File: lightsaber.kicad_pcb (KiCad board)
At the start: 2 copper layers, 31.5 x 127.8 mm, 9 parts, among them SW1 Button, SW2 POWER, U1 C3 Pico

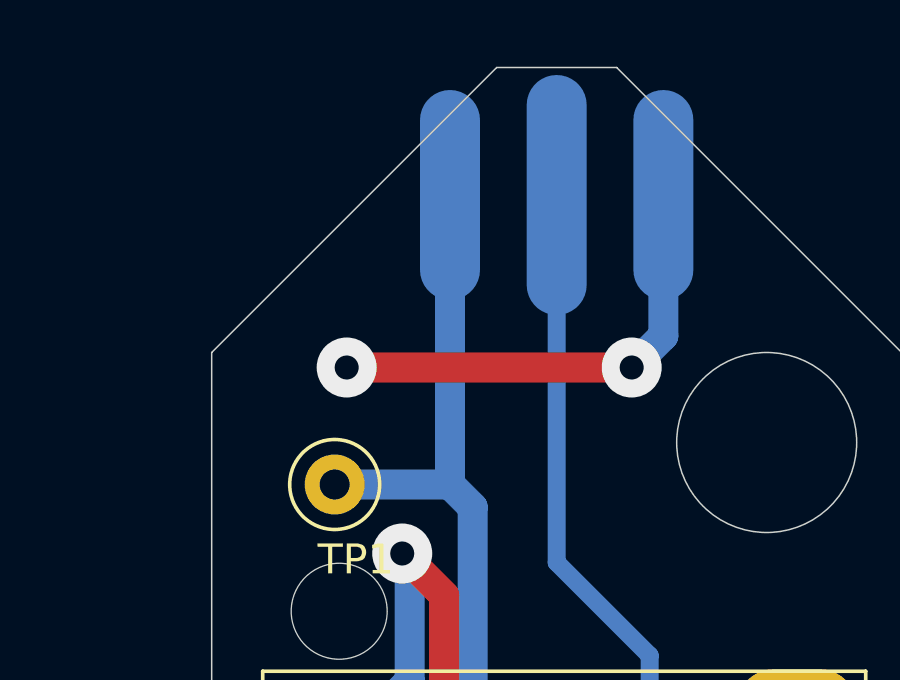
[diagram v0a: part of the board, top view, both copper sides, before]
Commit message: Make sure that the neopixel does not drain the battery so use 3V3 instead of VBAT
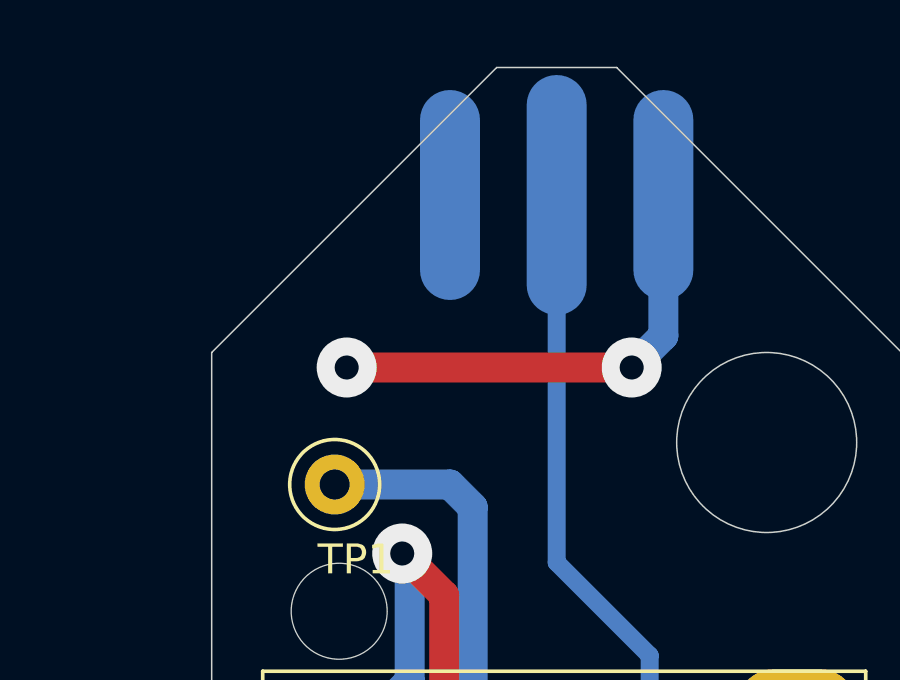
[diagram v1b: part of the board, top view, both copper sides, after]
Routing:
- net +4V: track 27.8 -> 18.1 mm
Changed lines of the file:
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@@
-	)
-	(segment
-		(start 116.944 48.65)
-		(end 116.944 39)
-		(width 1)
-		(layer "B.Cu")
-		(net 3)
 	)
 	(segment

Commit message: Specify light sensor and its resistor
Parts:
- R1: footprint OptoDevice:R_LDR_4.9x4.2mm_P2.54mm_Vertical -> OptoDevice:R_LDR_5.1x4.3mm_P3.4mm_Vertical
- R3: value 100k -> 47k
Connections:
- NP1 pad 1: +4V -> +3V3

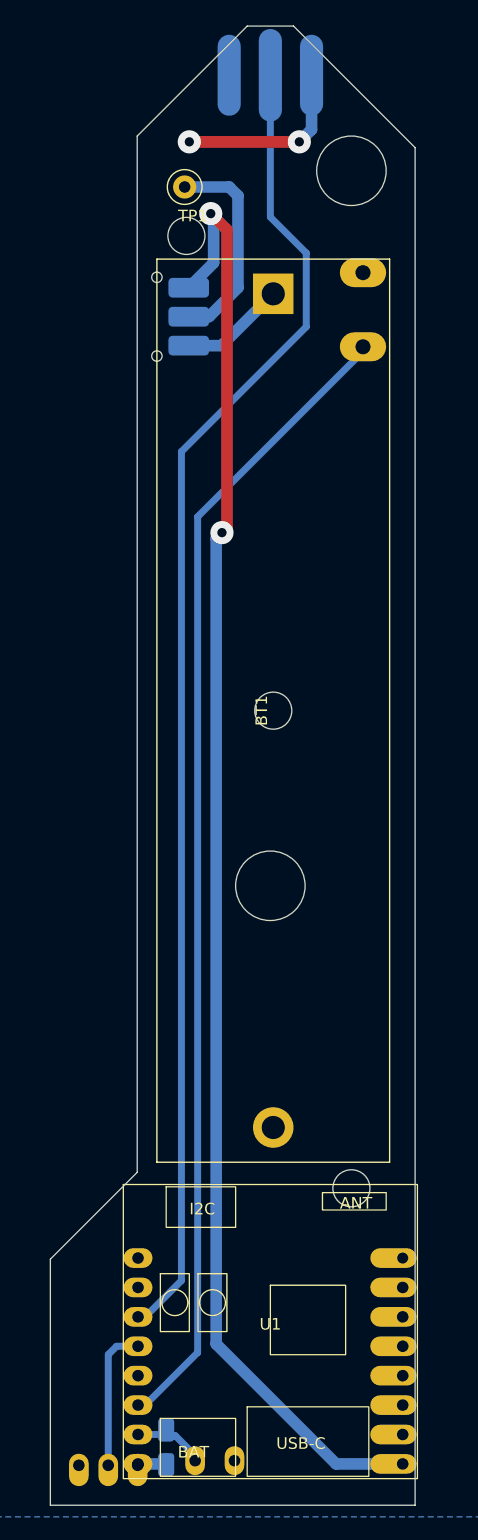
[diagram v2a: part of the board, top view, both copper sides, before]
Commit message: Change pinout, add m3 mounting holes
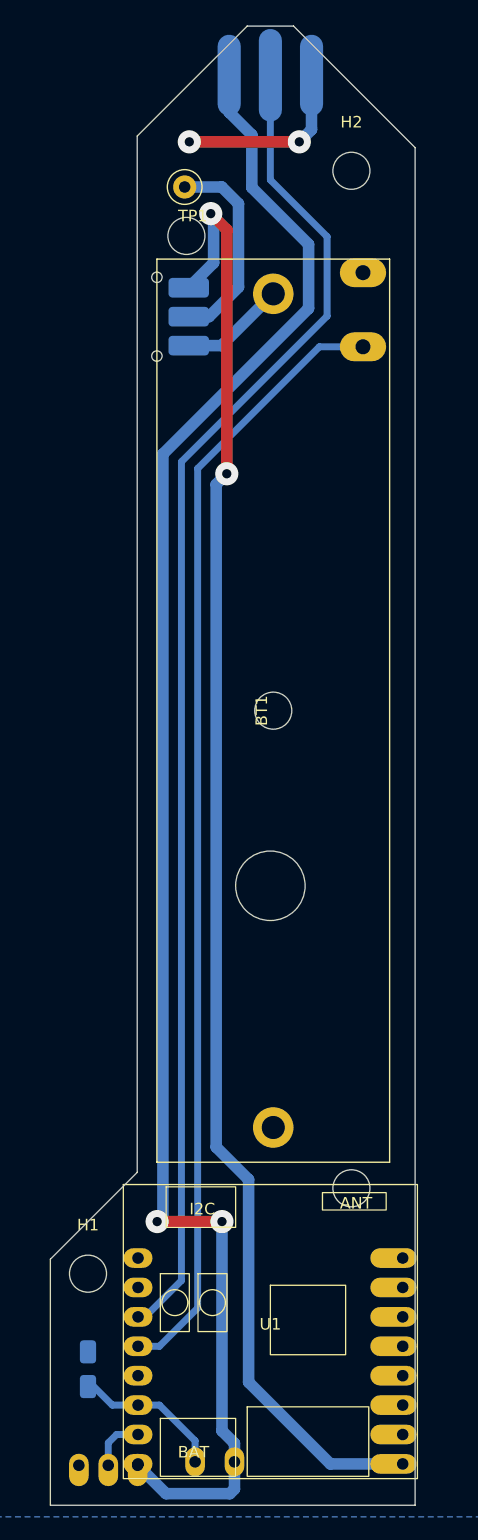
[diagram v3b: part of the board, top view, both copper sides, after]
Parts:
- added H1: MountingHole, MountingHole:MountingHole_3.2mm_M3, F.Cu at (104.8, 142.5)
- added H2: MountingHole, MountingHole:MountingHole_3.2mm_M3, F.Cu at (127.5, 47.2)
- moved R3 9.55 mm to (104.8, 150.8), turned to -90 degrees
- moved R1 0.10 mm to (114.0, 158.8)
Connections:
- R1 pad 2: GND -> +3V3
- R3 pad 1: +3V3 -> GND
- U1 pad 10: Light -> Poti
- U1 pad 11: Button -> Light
- U1 pad 13: Poti -> Button
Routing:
- net +3V3: track 2.65 -> 146.5 mm, vias 0 -> 2
- net Poti: track 12.8 -> 4.81 mm
- net Light: track 6.13 -> 13.5 mm
- net Button: track 99.8 -> 97.7 mm
- net Neopixel: track 114.9 -> 116.4 mm
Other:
- outline, holes or cut-outs redrawn

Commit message: Cleanup pcb
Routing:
- net +3V3: track 146.5 -> 151.6 mm, vias 2 -> 4
- removed copper zone on B.Cu, net +3V3
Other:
- board size 31.5 x 127.8 mm -> 31.5 x 126.2 mm
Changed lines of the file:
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@@
 	(gr_poly
 		(pts
-			(xy 133 162.5) (xy 101.5 162.5) (xy 101.5 141.25) (xy 109 133.75) (xy 109 44.25) (xy 118.5 34.75)
-			(xy 122.5 34.75) (xy 133 45.25)
+			(xy 133 161) (xy 101.5 161) (xy 101.5 141.25) (xy 109 133.75) (xy 109 44.25) (xy 118.5 34.75) (xy 122.5 34.75)
+			(xy 133 45.25)
 		)
 		(stroke
@@
 	)
 	(segment
+		(start 117.7 156.2)
+		(end 120.25 158.75)
+		(width 1)
+		(layer "F.Cu")
+		(net 11)
+	)
+	(segment
+		(start 111.35 159)
+		(end 111.35 157.9)
+		(width 1)
+		(layer "F.Cu")
+		(net 11)
+	)
+	(segment
 		(start 116.32 138)
 		(end 110.72 138)
@@
 		(net 11)
 	)
+	(segment
+		(start 113.05 156.2)
+		(end 117.7 156.2)
+		(width 1)
+		(layer "F.Cu")
+		(net 11)
+	)
+	(segment
+		(start 111.35 157.9)
+		(end 113.05 156.2)
+		(width 1)
+		(layer "F.Cu")
+		(net 11)
+	)
 	(via
 		(at 116.32 138)
+		(size 2)
+		(drill 0.8)
+		(layers "F.Cu" "B.Cu")
+		(net 11)
+	)
+	(via
+		(at 120.25 158.75)
+		(size 2)
+		(drill 0.8)
+		(layers "F.Cu" "B.Cu")
+		(net 11)
+	)
+	(via
+		(at 111.35 159)
 		(size 2)
 		(drill 0.8)
@@
 	)
 	(segment
+		(start 111.28 158.93)
+		(end 111.35 159)
+		(width 1)
+		(layer "B.Cu")
+		(net 11)
+	)
+	(segment
 		(start 109.04 158.96)
 		(end 109.07 158.93)
@@
 	)
 	(segment
-		(start 117 161.5)
-		(end 111.49 161.5)
+		(start 120.25 158.75)
+		(end 117.4 158.75)
 		(width 1)
 		(layer "B.Cu")
@@
 	)
 	(segment
+		(start 109.07 158.93)
+		(end 111.28 158.93)
+		(width 1)
+		(layer "B.Cu")
+		(net 11)
+	)
+	(segment
 		(start 118.9 48.700089)
 		(end 123.8 53.600089)
@@
 	)
 	(segment
-		(start 117.4 161.1)
-		(end 117 161.5)
-		(width 1)
-		(layer "B.Cu")
-		(net 11)
-	)
-	(segment
 		(start 123.8 53.600089)
 		(end 123.8 59.138352)
@@
 	)
 	(segment
-		(start 111.49 161.5)
-		(end 109.04 159.05)
-		(width 1)
-		(layer "B.Cu")
-		(net 11)
-	)
-	(segment
 		(start 116.944 42.194)
 		(end 118.9 44.15)
@@
 		(start 111.22 138)
 		(end 110.72 138)
-		(width 1)
-		(layer "B.Cu")
-		(net 11)
-	)
-	(segment
-		(start 117.4 158.75)
-		(end 117.4 161.1)
 		(width 1)
 		(layer "B.Cu")
@@
 			)
 		)
-	)
-	(zone
-		(net 11)
-		(net_name "+3V3")
-		(layer "B.Cu")
-		(hatch edge 0.5)
-		(priority 2)
-		(connect_pads yes
-			(clearance 0.5)
-		)
-		(min_thickness 0.25)
-		(filled_areas_thickness no)
-		(fill yes
-			(thermal_gap 0.5)
-			(thermal_bridge_width 0.5)
-		)
-		(polygon
-			(pts
-				(xy 170 145.75) (xy 175 145.75) (xy 175 149.75) (xy 170 149.75)
-			)
-		)

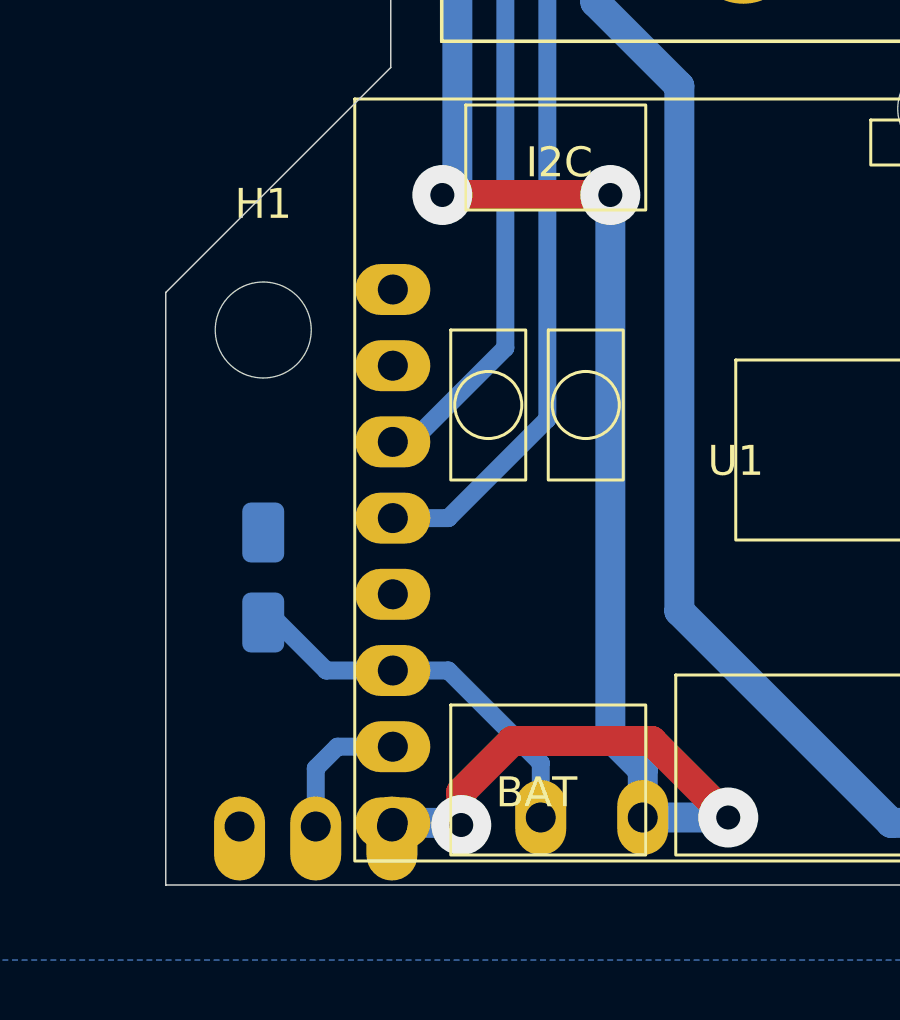
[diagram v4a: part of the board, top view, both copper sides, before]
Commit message: Fix pin 5 does not allow ADC
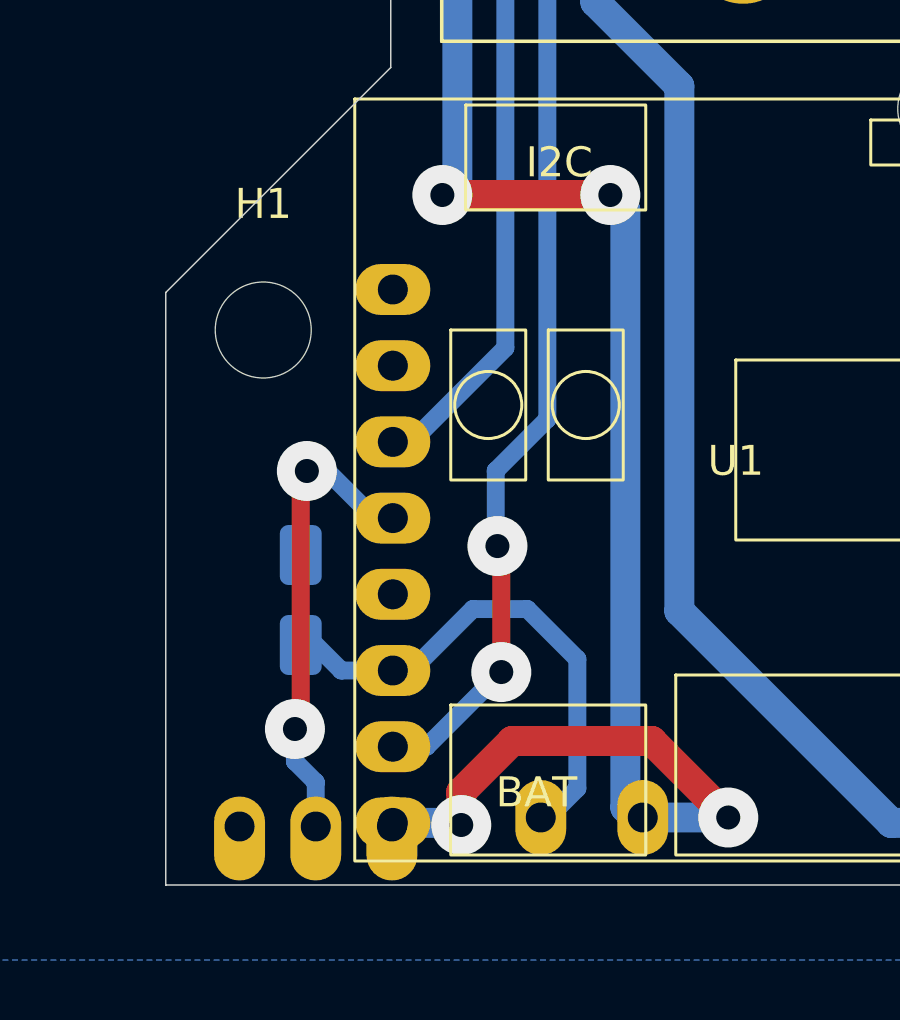
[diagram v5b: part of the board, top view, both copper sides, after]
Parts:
- moved R3 1.46 mm to (106.0, 151.5)
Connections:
- U1 pad 10: Poti -> Button
- U1 pad 13: Button -> Poti
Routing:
- net Poti: track 4.81 -> 15.8 mm, vias 0 -> 2
- net Button: track 97.7 -> 105.0 mm, vias 0 -> 2
- net Light: track 13.5 -> 17.4 mm
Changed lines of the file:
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@@
 			(layers "*.Cu" "*.Mask")
 			(remove_unused_layers no)
-			(net 12 "Poti")
+			(net 15 "Button")
 			(pinfunction "IO5")
 			(pintype "bidirectional")
@@
 			(layers "*.Cu" "*.Mask")
 			(remove_unused_layers no)
-			(net 15 "Button")
+			(net 12 "Poti")
 			(pinfunction "IO1/SCK")
 			(pintype "bidirectional")
@@
 	(footprint "Resistor_SMD:R_0805_2012Metric_Pad1.20x1.40mm_HandSolder"
 		(layer "B.Cu")
-		(at 104.75 150.75 -90)
+		(at 106 151.5 -90)
 		(descr "Resistor SMD 0805 (2012 Metric), square (rectangular) end terminal, IPC_7351 nominal with elongated pad for handsoldering. (Body size source: IPC-SM-782 page 72, https://www.pcb-3d.com/wordpress/wp-content/uploads/ipc-sm-782a_amendment_1_and_2.pdf), generated with kicad-footprint-generator")
 		(tags "resistor handsolder")
@@
 	)
 	(segment
-		(start 104.75 151.75)
-		(end 106.85 153.85)
+		(start 111.735576 151.80214)
+		(end 113.554215 151.80214)
 		(width 0.6)
 		(layer "B.Cu")
@@
 	)
 	(segment
+		(start 107.35 153.85)
+		(end 109.07 153.85)
+		(width 0.6)
+		(layer "B.Cu")
+		(net 9)
+	)
+	(segment
+		(start 115.22 157.78)
+		(end 114 159)
+		(width 0.6)
+		(layer "B.Cu")
+		(net 9)
+	)
+	(segment
+		(start 115.22 153.467925)
+		(end 115.22 157.78)
+		(width 0.6)
+		(layer "B.Cu")
+		(net 9)
+	)
+	(segment
+		(start 106 152.5)
+		(end 107.35 153.85)
+		(width 0.6)
+		(layer "B.Cu")
+		(net 9)
+	)
+	(segment
 		(start 109.07 153.85)
-		(end 110.92 153.85)
+		(end 109.687716 153.85)
 		(width 0.6)
 		(layer "B.Cu")
@@
 	)
 	(segment
-		(start 114 156.93)
-		(end 114 159)
+		(start 113.554215 151.80214)
+		(end 115.22 153.467925)
 		(width 0.6)
 		(layer "B.Cu")
@@
 	)
 	(segment
-		(start 106.85 153.85)
-		(end 109.07 153.85)
-		(width 0.6)
-		(layer "B.Cu")
-		(net 9)
-	)
-	(segment
-		(start 110.92 153.85)
-		(end 114 156.93)
+		(start 109.687716 153.85)
+		(end 111.735576 151.80214)
 		(width 0.6)
 		(layer "B.Cu")
@@
 	)
 	(segment
-		(start 116.32 138)
-		(end 116.32 156.07)
-		(width 1)
-		(layer "B.Cu")
-		(net 11)
-	)
-	(segment
 		(start 111.28 158.93)
 		(end 111.35 159)
@@
 	)
 	(segment
+		(start 116.82 138.5)
+		(end 116.82 158.42)
+		(width 1)
+		(layer "B.Cu")
+		(net 11)
+	)
+	(segment
+		(start 116.82 158.42)
+		(end 117.4 159)
+		(width 1)
+		(layer "B.Cu")
+		(net 11)
+	)
+	(segment
 		(start 109.04 158.96)
 		(end 109.07 158.93)
@@
 	)
 	(segment
-		(start 117.4 157.15)
-		(end 117.4 159)
-		(width 1)
-		(layer "B.Cu")
-		(net 11)
-	)
-	(segment
 		(start 109.07 158.93)
 		(end 111.28 158.93)
@@
 	)
 	(segment
-		(start 116.32 156.07)
-		(end 117.4 157.15)
+		(start 116.32 138)
+		(end 116.82 138.5)
 		(width 1)
 		(layer "B.Cu")
@@
 	)
 	(segment
-		(start 106.5 157.11)
+		(start 106.20391 147.200001)
+		(end 106 147.403911)
+		(width 0.6)
+		(layer "F.Cu")
+		(net 12)
+	)
+	(segment
+		(start 106 147.403911)
+		(end 106 155.606157)
+		(width 0.6)
+		(layer "F.Cu")
+		(net 12)
+	)
+	(segment
+		(start 106 155.606157)
+		(end 105.806157 155.8)
+		(width 0.6)
+		(layer "F.Cu")
+		(net 12)
+	)
+	(via
+		(at 106.20391 147.200001)
+		(size 2)
+		(drill 0.8)
+		(layers "F.Cu" "B.Cu")
+		(net 12)
+	)
+	(via
+		(at 105.806157 155.8)
+		(size 2)
+		(drill 0.8)
+		(layers "F.Cu" "B.Cu")
+		(net 12)
+	)
+	(segment
+		(start 105.806157 156.880878)
+		(end 106.5 157.574721)
+		(width 0.6)
+		(layer "B.Cu")
+		(net 12)
+	)
+	(segment
+		(start 105.806157 155.8)
+		(end 105.806157 156.880878)
+		(width 0.6)
+		(layer "B.Cu")
+		(net 12)
+	)
+	(segment
+		(start 106.5 157.574721)
 		(end 106.5 159.05)
 		(width 0.6)
@@
 	)
 	(segment
-		(start 107.22 156.39)
-		(end 106.5 157.11)
+		(start 108.452284 148.77)
+		(end 109.07 148.77)
 		(width 0.6)
 		(layer "B.Cu")
@@
 	)
 	(segment
-		(start 109.07 156.39)
-		(end 107.22 156.39)
+		(start 106.20391 147.200001)
+		(end 106.882285 147.200001)
+		(width 0.6)
+		(layer "B.Cu")
+		(net 12)
+	)
+	(segment
+		(start 106.882285 147.200001)
+		(end 108.452284 148.77)
 		(width 0.6)
 		(layer "B.Cu")
@@
 	)
 	(segment
+		(start 112.555622 149.70214)
+		(end 112.684366 149.830884)
+		(width 0.6)
+		(layer "F.Cu")
+		(net 15)
+	)
+	(segment
+		(start 112.684366 149.830884)
+		(end 112.684366 153.90214)
+		(width 0.6)
+		(layer "F.Cu")
+		(net 15)
+	)
+	(via
+		(at 112.555622 149.70214)
+		(size 2)
+		(drill 0.8)
+		(layers "F.Cu" "B.Cu")
+		(net 15)
+	)
+	(via
+		(at 112.684366 153.90214)
+		(size 2)
+		(drill 0.8)
+		(layers "F.Cu" "B.Cu")
+		(net 15)
+	)
+	(segment
 		(start 124.730992 62.45)
 		(end 128.5 62.45)
@@
 	)
 	(segment
+		(start 112.5 147.19)
+		(end 114.22 145.47)
+		(width 0.6)
+		(layer "B.Cu")
+		(net 15)
+	)
+	(segment
+		(start 112.5 149.646518)
+		(end 112.5 147.19)
+		(width 0.6)
+		(layer "B.Cu")
+		(net 15)
+	)
+	(segment
 		(start 114.22 145.47)
 		(end 114.22 72.960992)
@@
 	)
 	(segment
+		(start 110.196506 156.39)
+		(end 112.684366 153.90214)
+		(width 0.6)
+		(layer "B.Cu")
+		(net 15)
+	)
+	(segment
+		(start 109.07 156.39)
+		(end 110.196506 156.39)
+		(width 0.6)
+		(layer "B.Cu")
+		(net 15)
+	)
+	(segment
+		(start 112.555622 149.70214)
+		(end 112.5 149.646518)
+		(width 0.6)
+		(layer "B.Cu")
+		(net 15)
+	)
+	(segment
 		(start 114.22 72.960992)
 		(end 124.730992 62.45)
 		(width 0.6)
 		(layer "B.Cu")
-		(net 15)
-	)
-	(segment
-		(start 109.07 148.77)
-		(end 110.92 148.77)
-		(width 0.6)
-		(layer "B.Cu")
-		(net 15)
-	)
-	(segment
-		(start 110.92 148.77)
-		(end 114.22 145.47)
-		(width 0.6)
-		(layer "B.Cu")
